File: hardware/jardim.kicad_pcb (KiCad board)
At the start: 2 copper layers, 100 x 100 mm, 91 parts, among them J1 DC_INPUT, J10 DHT22_AMB, J11 LIGHT_SENSOR_1, J12 LIGHT_SENSOR_2, J13 LEVEL_SENSOR_1, J14 LEVEL_SENSOR_2, J15 SOIL_HUMIDITY_SENSOR_1, J16 SOIL_HUMIDITY_SENSOR_2, J18 USB_C_Receptacle_PowerOnly_6P, J2 PUMP_1, J3 PUMP_2, J4 LIGHT_1, J5 LIGHG_2, J6 HEAT_1, J7 HEAT_2, J8 DS12B20_2, J9 DS18B20_1, Q1 FQP30N06L, Q2 FQP30N06L, Q3 FQP30N06L, Q4 FQP30N06L, Q5 FQP30N06L, Q6 FQP30N06L, Q7 BC337, SW1 SW_Push, SW2 SW_Push, SW3 SW_Push, SW4 SW_SPST, U1 AM2302, U2 DM-OLED096-636

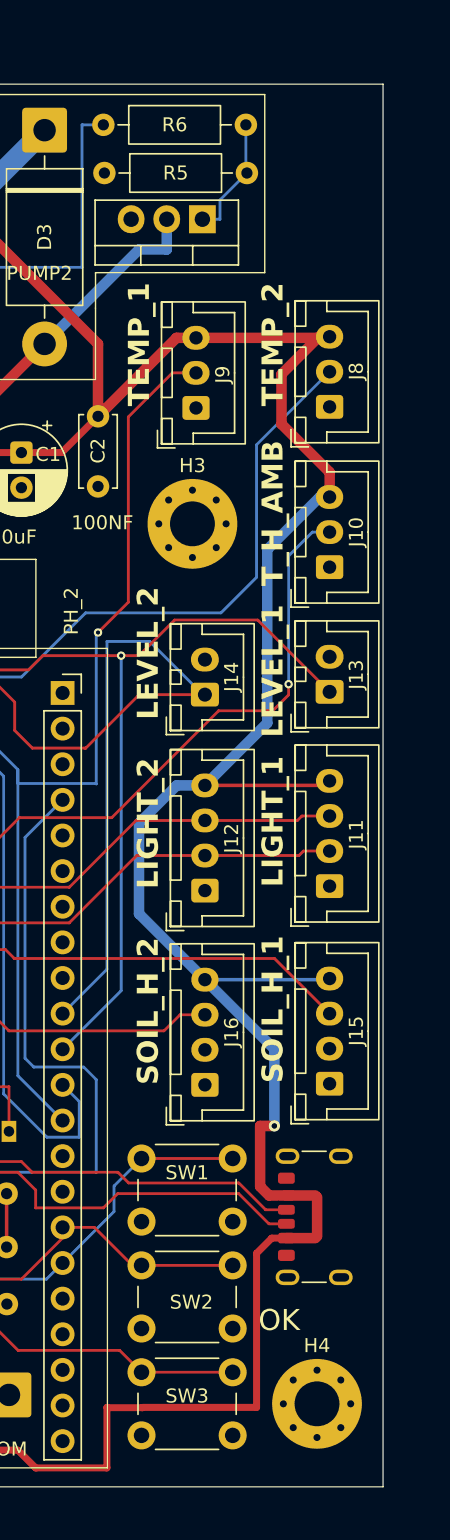
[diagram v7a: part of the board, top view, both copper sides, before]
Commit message: mudando o furo de lugar
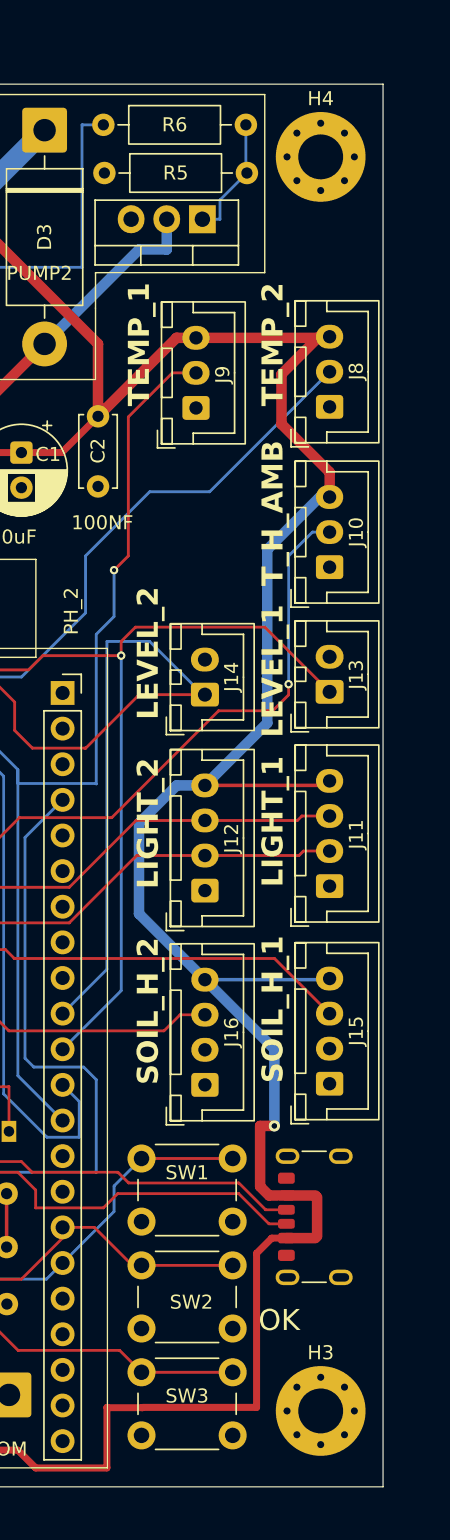
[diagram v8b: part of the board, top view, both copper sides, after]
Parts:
- moved H4 88.9 mm to (188.0, 43.2)
- moved H3 63.9 mm to (188.0, 132.6)
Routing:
- net /IO36: track 85.1 -> 81.9 mm
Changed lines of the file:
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@@
 	(footprint "MountingHole:MountingHole_3.2mm_M3_Pad_Via"
 		(layer "F.Cu")
-		(at 187.6973 132.08)
+		(at 187.96 43.18)
 		(descr "Mounting Hole 3.2mm, M3, generated by kicad-footprint-generator mountinghole.py")
 		(tags "mountinghole M3")
@@
 	(footprint "MountingHole:MountingHole_3.2mm_M3_Pad_Via"
 		(layer "F.Cu")
-		(at 178.816 69.342)
+		(at 187.96 132.588)
 		(descr "Mounting Hole 3.2mm, M3, generated by kicad-footprint-generator mountinghole.py")
 		(tags "mountinghole M3")
@@
 	)
 	(segment
-		(start 161.586 80.264)
-		(end 159.935 81.915)
+		(start 171.196 71.628)
+		(end 171.196 75.692)
 		(width 0.2)
 		(layer "B.Cu")
@@
 	)
 	(segment
-		(start 188.595 58.5)
-		(end 183.388 63.707)
+		(start 168.442 113.07)
+		(end 165.354 109.982)
 		(width 0.2)
 		(layer "B.Cu")
@@
 	)
 	(segment
-		(start 183.388 63.707)
-		(end 183.388 73.152)
+		(start 166.624 80.264)
+		(end 161.586 80.264)
 		(width 0.2)
 		(layer "B.Cu")
@@
 	)
 	(segment
-		(start 168.442 113.07)
-		(end 165.354 109.982)
+		(start 169.56 109.34)
+		(end 170.7449 110.5249)
 		(width 0.2)
 		(layer "B.Cu")
@@
 	)
 	(segment
-		(start 180.848 75.692)
-		(end 171.196 75.692)
+		(start 165.354 87.334)
+		(end 159.935 81.915)
 		(width 0.2)
 		(layer "B.Cu")
@@
 	)
 	(segment
-		(start 169.56 109.34)
-		(end 170.7449 110.5249)
+		(start 170.7449 113.07)
+		(end 168.442 113.07)
 		(width 0.2)
 		(layer "B.Cu")
@@
 	)
 	(segment
-		(start 165.354 87.334)
+		(start 161.586 80.264)
 		(end 159.935 81.915)
 		(width 0.2)
@@
 	)
 	(segment
-		(start 170.7449 113.07)
-		(end 168.442 113.07)
+		(start 171.196 75.692)
+		(end 166.624 80.264)
 		(width 0.2)
 		(layer "B.Cu")
@@
 	)
 	(segment
-		(start 171.196 75.692)
-		(end 166.624 80.264)
+		(start 165.354 109.982)
+		(end 165.354 87.334)
 		(width 0.2)
 		(layer "B.Cu")
@@
 	)
 	(segment
-		(start 183.388 73.152)
-		(end 180.848 75.692)
+		(start 188.595 58.5)
+		(end 180.039 67.056)
 		(width 0.2)
 		(layer "B.Cu")
@@
 	)
 	(segment
-		(start 165.354 109.982)
-		(end 165.354 87.334)
+		(start 175.768 67.056)
+		(end 171.196 71.628)
 		(width 0.2)
 		(layer "B.Cu")
@@
 	)
 	(segment
-		(start 166.624 80.264)
-		(end 161.586 80.264)
+		(start 180.039 67.056)
+		(end 175.768 67.056)
 		(width 0.2)
 		(layer "B.Cu")
@@
 	)
 	(segment
-		(start 173.736 78.74)
-		(end 175.006 78.74)
+		(start 158.919 79.756)
+		(end 156.76 81.915)
 		(width 0.2)
 		(layer "F.Cu")
@@
 	)
 	(segment
-		(start 177.546 76.2)
-		(end 183.475 76.2)
+		(start 173.736 77.724)
+		(end 174.752 76.708)
 		(width 0.2)
 		(layer "F.Cu")
@@
 	)
 	(segment
-		(start 167.132 79.756)
-		(end 158.919 79.756)
+		(start 173.736 78.74)
+		(end 173.736 77.724)
 		(width 0.2)
 		(layer "F.Cu")
@@
 	)
 	(segment
-		(start 175.006 78.74)
-		(end 177.546 76.2)
+		(start 173.736 78.74)
+		(end 168.148 78.74)
 		(width 0.2)
 		(layer "F.Cu")
@@
 	)
 	(segment
-		(start 183.475 76.2)
+		(start 183.983 76.708)
 		(end 188.595 81.32)
 		(width 0.2)
@@
 	)
 	(segment
-		(start 158.919 79.756)
-		(end 156.76 81.915)
+		(start 167.132 79.756)
+		(end 158.919 79.756)
 		(width 0.2)
 		(layer "F.Cu")
@@
 	)
 	(segment
-		(start 173.736 78.74)
-		(end 168.148 78.74)
+		(start 174.752 76.708)
+		(end 183.983 76.708)
 		(width 0.2)
 		(layer "F.Cu")
@@
 	)
 	(segment
-		(start 174.244 74.93)
-		(end 174.244 61.722)
+		(start 174.244 61.722)
+		(end 177.386 58.58)
 		(width 0.2)
 		(layer "F.Cu")
@@
 	)
 	(segment
-		(start 177.386 58.58)
-		(end 179.07 58.58)
+		(start 174.244 71.628)
+		(end 174.244 61.722)
 		(width 0.2)
 		(layer "F.Cu")
@@
 	)
 	(segment
-		(start 172.085 77.089)
-		(end 174.244 74.93)
+		(start 173.228 72.644)
+		(end 174.244 71.628)
 		(width 0.2)
 		(layer "F.Cu")
@@
 	)
 	(segment
-		(start 174.244 61.722)
-		(end 177.386 58.58)
+		(start 177.386 58.58)
+		(end 179.07 58.58)
 		(width 0.2)
 		(layer "F.Cu")
@@
 	)
 	(via
-		(at 172.085 77.089)
+		(at 173.228 72.644)
 		(size 0.6)
 		(drill 0.3)
@@
 	)
 	(segment
-		(start 171.958 77.216)
-		(end 171.958 87.884)
+		(start 163.322 81.788)
+		(end 163.195 81.915)
 		(width 0.2)
 		(layer "B.Cu")
@@
 	)
 	(segment
-		(start 163.322 81.788)
-		(end 163.195 81.915)
+		(start 163.195 81.915)
+		(end 163.322 82.042)
 		(width 0.2)
 		(layer "B.Cu")
@@
 	)
 	(segment
-		(start 171.958 87.884)
-		(end 171.93 87.856)
+		(start 166.37 86.868)
+		(end 166.37 108.69)
 		(width 0.2)
 		(layer "B.Cu")
@@
 	)
 	(segment
-		(start 163.195 81.915)
-		(end 163.322 82.042)
+		(start 163.322 82.042)
+		(end 163.322 83.82)
 		(width 0.2)
 		(layer "B.Cu")
@@
 	)
 	(segment
-		(start 166.37 87.856)
-		(end 166.37 86.868)
+		(start 171.958 77.216)
+		(end 171.958 87.884)
 		(width 0.2)
 		(layer "B.Cu")
@@
 	)
 	(segment
-		(start 166.37 86.868)
-		(end 166.37 108.69)
+		(start 166.37 108.69)
+		(end 169.56 111.88)
 		(width 0.2)
 		(layer "B.Cu")
@@
 	)
 	(segment
-		(start 163.322 82.042)
-		(end 163.322 83.82)
+		(start 171.958 87.884)
+		(end 171.93 87.856)
 		(width 0.2)
 		(layer "B.Cu")
@@
 	)
 	(segment
-		(start 166.37 108.69)
-		(end 169.56 111.88)
+		(start 166.37 87.856)
+		(end 166.37 86.868)
+		(width 0.2)
+		(layer "B.Cu")
+		(net "/IO35")
+	)
+	(segment
+		(start 166.37 86.868)
+		(end 163.322 83.82)
 		(width 0.2)
 		(layer "B.Cu")
@@
 	)
 	(segment
-		(start 166.37 86.868)
-		(end 163.322 83.82)
+		(start 173.228 75.946)
+		(end 171.958 77.216)
 		(width 0.2)
 		(layer "B.Cu")
@@
 	)
 	(segment
-		(start 172.085 77.089)
-		(end 171.958 77.216)
+		(start 173.228 72.644)
+		(end 173.228 75.946)
 		(width 0.2)
 		(layer "B.Cu")
